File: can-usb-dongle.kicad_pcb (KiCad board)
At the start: 2 copper layers, 30 x 15 mm, 43 parts, among them SW1 SW_PUSH, U1 STM32F302C8T, U2 SN65HVD256, U3 NUF2042XV6, U4 MCP1700, U5 SiP32431, X1 16MHz 10ppm

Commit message: Modify silkscreen text
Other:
- board text added: "CVRA CAN to USB dongle Rev A"
- board text removed: "CAN to USB dongle - Rev A"
- board text removed: "CVRA"
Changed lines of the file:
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@@
     (links 115)
     (no_connects 6)
-    (area 25.087299 28.495199 91.421702 60.2)
+    (area 44.899999 37.399999 75.100001 52.600001)
     (thickness 1.6)
-    (drawings 22)
+    (drawings 21)
     (tracks 470)
     (zones 0)
@@
       (net 10 "Net-(CONN3-Pad6)") (solder_mask_margin 0.2) (clearance 0.3))
   )
-  (gr_text CVRA (at 52.1 51.2 180) (layer B.SilkS)
-    (effects (font (size 0.8 0.8) (thickness 0.2)) (justify mirror))
-  )
   (gr_line (start 46.3 51.15) (end 45.7 51.15) (layer B.SilkS) (width 0.15))
   (gr_line (start 46 50.85) (end 46.3 51.15) (layer B.SilkS) (width 0.15))
@@
     (effects (font (size 0.8 0.8) (thickness 0.2)) (justify mirror))
   )
-  (gr_text "CAN to USB dongle - Rev A" (at 45.75 38.75 180) (layer B.SilkS)
+  (gr_text "CVRA CAN to USB dongle Rev A" (at 45.75 38.75 180) (layer B.SilkS)
     (effects (font (size 0.8 0.8) (thickness 0.15)) (justify left mirror))
   )
-  (gr_text + (at 54.25 50.25) (layer B.SilkS)
-    (effects (font (size 1.5 1.5) (thickness 0.3)) (justify mirror))
+  (gr_text + (at 55.75 51.75) (layer B.SilkS)
+    (effects (font (size 1 1) (thickness 0.2)) (justify mirror))
   )
   (gr_text "+ - TX RX" (at 71.25 38.5 180) (layer B.SilkS)

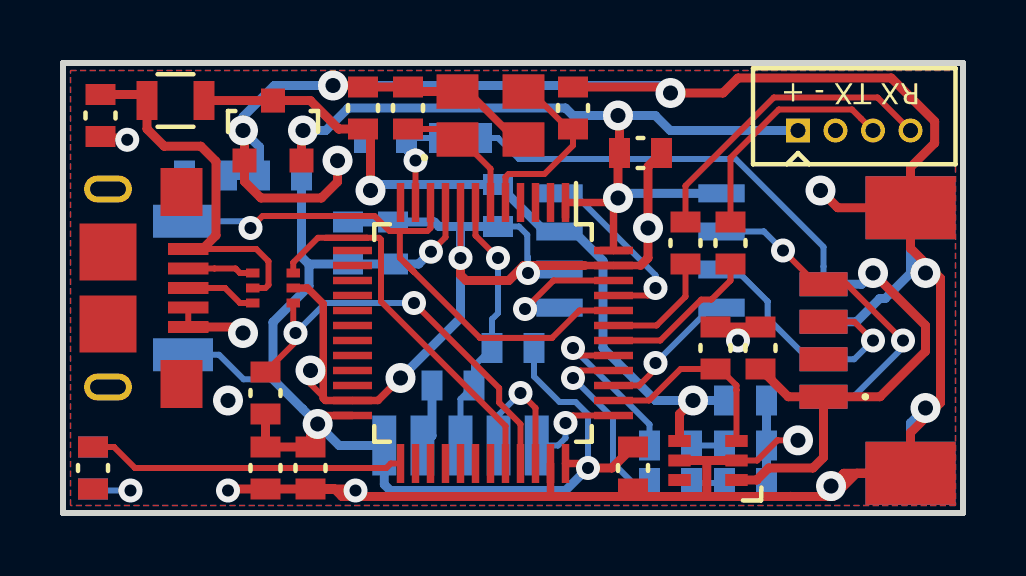
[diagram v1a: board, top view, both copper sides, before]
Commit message: Update footprints (USB, voltage regulator)
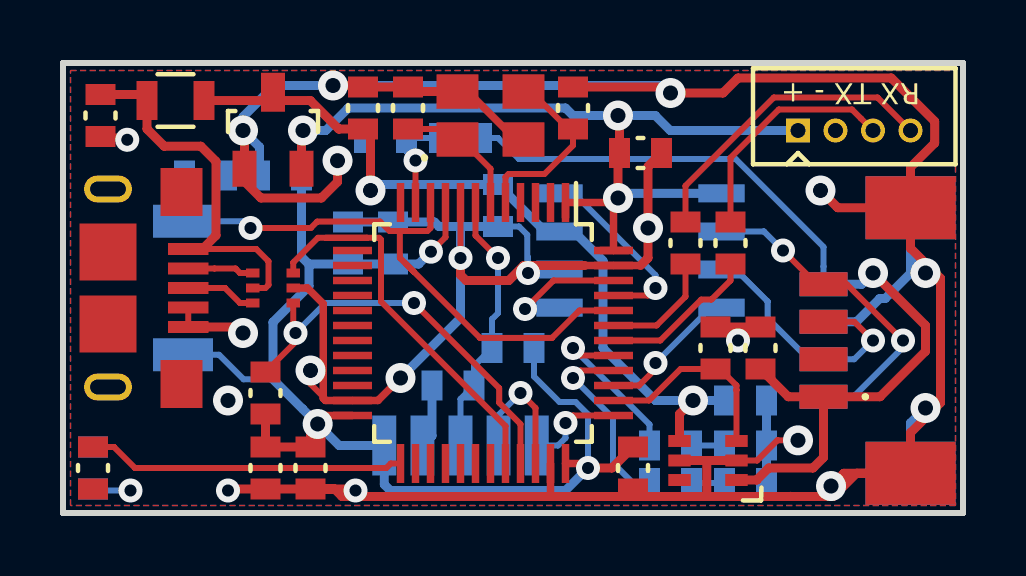
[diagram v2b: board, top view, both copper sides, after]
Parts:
- U4: footprint Housings_SOT-23_SOT-143_TSOT-6:SOT-23 -> _std:SOT-23
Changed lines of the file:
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@@
     (links 115)
     (no_connects 6)
-    (area 44.899999 37.399999 75.100001 52.600001)
+    (area 25.087299 28.495199 91.421702 60.2)
     (thickness 1.6)
     (drawings 21)
-    (tracks 470)
+    (tracks 471)
     (zones 0)
     (modules 43)
@@
       (net 7 "Net-(C13-Pad1)"))
     (model Resistors_SMD.3dshapes/R_0805.wrl
-      (at (xyz 0 0 0))
-      (scale (xyz 1 1 1))
-      (rotate (xyz 0 0 0))
-    )
-  )
-  (module Housings_SOT-23_SOT-143_TSOT-6:SOT-23 (layer F.Cu)
-    (at 52 39.75)
-    (descr "SOT-23, Standard")
-    (tags SOT-23)
-    (attr smd)
-    (fp_text reference U4 (at 0 -2.25) (layer F.SilkS) hide
-      (effects (font (size 1 1) (thickness 0.15)))
-    )
-    (fp_text value MCP1700 (at 0 2.3) (layer F.Fab) hide
-      (effects (font (size 1 1) (thickness 0.15)))
-    )
-    (fp_line (start -1.65 -1.6) (end 1.65 -1.6) (layer F.CrtYd) (width 0.05))
-    (fp_line (start 1.65 -1.6) (end 1.65 1.6) (layer F.CrtYd) (width 0.05))
-    (fp_line (start 1.65 1.6) (end -1.65 1.6) (layer F.CrtYd) (width 0.05))
-    (fp_line (start -1.65 1.6) (end -1.65 -1.6) (layer F.CrtYd) (width 0.05))
-    (fp_line (start 1.29916 -0.65024) (end 1.2509 -0.65024) (layer F.SilkS) (width 0.15))
-    (fp_line (start -1.49982 0.0508) (end -1.49982 -0.65024) (layer F.SilkS) (width 0.15))
-    (fp_line (start -1.49982 -0.65024) (end -1.2509 -0.65024) (layer F.SilkS) (width 0.15))
-    (fp_line (start 1.29916 -0.65024) (end 1.49982 -0.65024) (layer F.SilkS) (width 0.15))
-    (fp_line (start 1.49982 -0.65024) (end 1.49982 0.0508) (layer F.SilkS) (width 0.15))
-    (pad 1 smd rect (at -0.95 1.00076) (size 0.8001 0.8001) (layers F.Cu F.Paste F.Mask)
-      (net 2 GND))
-    (pad 2 smd rect (at 0.95 1.00076) (size 0.8001 0.8001) (layers F.Cu F.Paste F.Mask)
-      (net 1 VCC))
-    (pad 3 smd rect (at 0 -0.99822) (size 0.8001 0.8001) (layers F.Cu F.Paste F.Mask)
-      (net 6 /V_USB))
-    (model Housings_SOT-23_SOT-143_TSOT-6.3dshapes/SOT-23.wrl
       (at (xyz 0 0 0))
       (scale (xyz 1 1 1))
@@
     (pad 6 thru_hole oval (at -3.3 0 270) (size 0.9 1.6) (drill oval 0.5 1.2) (layers *.Cu *.Mask)
       (net 10 "Net-(CONN3-Pad6)") (solder_mask_margin 0.2) (clearance 0.3))
+  )
+  (module _std:SOT-23 (layer F.Cu)
+    (at 52 39.75)
+    (descr "SOT-23, Standard")
+    (tags SOT-23)
+    (attr smd)
+    (fp_text reference U4 (at 0 -3) (layer F.SilkS) hide
+      (effects (font (size 1 1) (thickness 0.15)))
+    )
+    (fp_text value MCP1700 (at 0 3) (layer F.Fab)
+      (effects (font (size 1 1) (thickness 0.15)))
+    )
+    (fp_line (start 1.29916 -0.65024) (end 1.2509 -0.65024) (layer F.SilkS) (width 0.15))
+    (fp_line (start -1.49982 0.0508) (end -1.49982 -0.65024) (layer F.SilkS) (width 0.15))
+    (fp_line (start -1.49982 -0.65024) (end -1.2509 -0.65024) (layer F.SilkS) (width 0.15))
+    (fp_line (start 1.29916 -0.65024) (end 1.49982 -0.65024) (layer F.SilkS) (width 0.15))
+    (fp_line (start 1.49982 -0.65024) (end 1.49982 0.0508) (layer F.SilkS) (width 0.15))
+    (pad 1 smd rect (at -0.95 1.275) (size 0.8 1.2) (layers F.Cu F.Paste F.Mask)
+      (net 2 GND))
+    (pad 2 smd rect (at 0.95 1.275) (size 0.8 1.2) (layers F.Cu F.Paste F.Mask)
+      (net 1 VCC))
+    (pad 3 smd rect (at 0 -1.275) (size 0.8 1.3) (layers F.Cu F.Paste F.Mask)
+      (net 6 /V_USB))
+    (model Housings_SOT-23_SOT-143_TSOT-6.3dshapes/SOT-23.wrl
+      (at (xyz 0 0 0))
+      (scale (xyz 1 1 1))
+      (rotate (xyz 0 0 0))
+    )
   )
   (gr_line (start 46.3 51.15) (end 45.7 51.15) (layer B.SilkS) (width 0.15))
@@
   (segment (start 47.4 51) (end 55.775 51) (width 0.2) (layer F.Cu) (net 13))
   (segment (start 55.925 50.85) (end 56.25 50.85) (width 0.2) (layer F.Cu) (net 13))
+  (segment (start 55.884999 43.100001) (end 55.570568 42.78557) (width 0.2) (layer F.Cu) (net 14))
+  (segment (start 51.25 43) (end 53.259301 43) (width 0.2) (layer F.Cu) (net 14))
+  (segment (start 53.259301 43) (end 53.473731 42.78557) (width 0.2) (layer F.Cu) (net 14))
+  (segment (start 53.473731 42.78557) (end 55.570568 42.78557) (width 0.2) (layer F.Cu) (net 14))
   (segment (start 56.229049 43.100001) (end 55.884999 43.100001) (width 0.2) (layer F.Cu) (net 14))
   (segment (start 57.149999 43.100001) (end 56.229049 43.100001) (width 0.2) (layer F.Cu) (net 14))
@@
   (segment (start 49 42.775) (end 51.025 42.775) (width 0.2) (layer B.Cu) (net 14))
   (segment (start 51.025 42.775) (end 51.25 43) (width 0.2) (layer B.Cu) (net 14))
-  (segment (start 55.884999 43.100001) (end 55.384999 42.600001) (width 0.2) (layer F.Cu) (net 14))
-  (segment (start 55.384999 42.600001) (end 51.649999 42.600001) (width 0.2) (layer F.Cu) (net 14))
-  (segment (start 51.649999 42.600001) (end 51.25 43) (width 0.2) (layer F.Cu) (net 14))
   (segment (start 57.149999 43.100001) (end 57.25 43) (width 0.2) (layer F.Cu) (net 14))
   (segment (start 57.25 43) (end 57.25 42.15) (width 0.2) (layer F.Cu) (net 14))

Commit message: Resolve GPIO conflict with JTAG pin
V_BUS_ENABLE and CAN_SILENT were in conflict with JTAG output pins.
They had to be moved because at boot time the output value cannot be guaranteed.
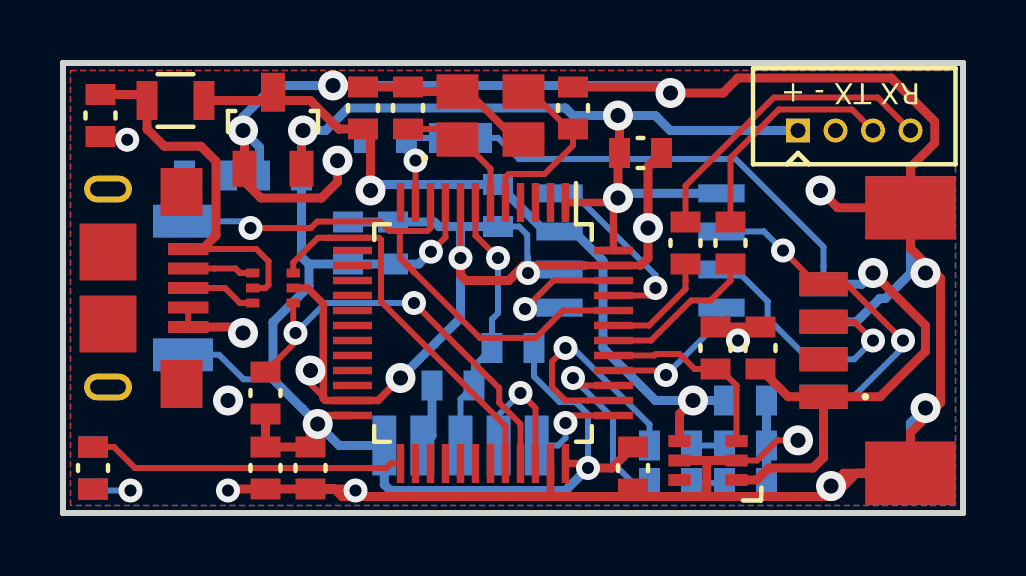
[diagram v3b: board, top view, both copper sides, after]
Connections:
- U1 pad 38: /V_BUS_ENABLE -> /CAN1_PWR_LED
- U1 pad 39: /CAN_SILENT -> /CAN1_STATUS_LED
- U1 pad 40: /CAN1_STATUS_LED -> /CAN_SILENT
- U1 pad 41: /CAN1_PWR_LED -> /V_BUS_ENABLE
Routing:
- net /CAN1_PWR_LED: track 5.76 -> 8.28 mm
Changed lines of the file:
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@@
     (links 115)
     (no_connects 6)
-    (area 25.087299 28.495199 91.421702 60.2)
+    (area 44.899999 37.399999 75.100001 52.600001)
     (thickness 1.6)
     (drawings 21)
-    (tracks 471)
+    (tracks 475)
     (zones 0)
     (modules 43)
@@
       (net 8 /SWCLK))
     (pad 38 smd rect (at 2.25 -4.35) (size 1.3 0.25) (layers F.Cu F.Paste F.Mask)
+      (net 27 /CAN1_PWR_LED))
+    (pad 39 smd rect (at 1.75 -4.35) (size 1.3 0.25) (layers F.Cu F.Paste F.Mask)
+      (net 26 /CAN1_STATUS_LED))
+    (pad 40 smd rect (at 1.25 -4.35) (size 1.3 0.25) (layers F.Cu F.Paste F.Mask)
+      (net 24 /CAN_SILENT))
+    (pad 41 smd rect (at 0.75 -4.35) (size 1.3 0.25) (layers F.Cu F.Paste F.Mask)
       (net 17 /V_BUS_ENABLE))
-    (pad 39 smd rect (at 1.75 -4.35) (size 1.3 0.25) (layers F.Cu F.Paste F.Mask)
-      (net 24 /CAN_SILENT))
-    (pad 40 smd rect (at 1.25 -4.35) (size 1.3 0.25) (layers F.Cu F.Paste F.Mask)
-      (net 26 /CAN1_STATUS_LED))
-    (pad 41 smd rect (at 0.75 -4.35) (size 1.3 0.25) (layers F.Cu F.Paste F.Mask)
-      (net 27 /CAN1_PWR_LED))
     (pad 42 smd rect (at 0.25 -4.35) (size 1.3 0.25) (layers F.Cu F.Paste F.Mask)
       (net 21 /UART1_TX))
@@
   (segment (start 47.4 51) (end 55.775 51) (width 0.2) (layer F.Cu) (net 13))
   (segment (start 55.925 50.85) (end 56.25 50.85) (width 0.2) (layer F.Cu) (net 13))
+  (segment (start 60.760083 46.663999) (end 58.900001 46.663999) (width 0.2) (layer F.Cu) (net 14))
+  (segment (start 63.35 45.75) (end 61.674082 45.75) (width 0.2) (layer F.Cu) (net 14))
+  (segment (start 61.674082 45.75) (end 60.760083 46.663999) (width 0.2) (layer F.Cu) (net 14))
+  (segment (start 58.900001 46.663999) (end 56.689849 44.453847) (width 0.2) (layer F.Cu) (net 14))
   (segment (start 55.884999 43.100001) (end 55.570568 42.78557) (width 0.2) (layer F.Cu) (net 14))
   (segment (start 51.25 43) (end 53.259301 43) (width 0.2) (layer F.Cu) (net 14))
@@
   (segment (start 56.229049 43.100001) (end 55.884999 43.100001) (width 0.2) (layer F.Cu) (net 14))
   (segment (start 57.149999 43.100001) (end 56.229049 43.100001) (width 0.2) (layer F.Cu) (net 14))
-  (segment (start 58.900001 46.663999) (end 56.689849 44.453847) (width 0.2) (layer F.Cu) (net 14))
   (segment (start 56.689849 44.453847) (end 56.4234 44.187398) (width 0.2) (layer F.Cu) (net 14))
   (segment (start 56.229049 43.100001) (end 56.229049 43.993047) (width 0.2) (layer F.Cu) (net 14))
   (segment (start 56.229049 43.993047) (end 56.689849 44.453847) (width 0.2) (layer F.Cu) (net 14))
-  (segment (start 63.35 45.75) (end 62.213998 45.75) (width 0.2) (layer F.Cu) (net 14))
-  (segment (start 62.213998 45.75) (end 61.299999 46.663999) (width 0.2) (layer F.Cu) (net 14))
-  (segment (start 61.299999 46.663999) (end 58.900001 46.663999) (width 0.2) (layer F.Cu) (net 14))
   (segment (start 49.05 41.25) (end 49.05 42.725) (width 0.2) (layer B.Cu) (net 14))
   (segment (start 49.05 42.725) (end 49 42.775) (width 0.2) (layer B.Cu) (net 14))
@@
   (segment (start 52.675 46.425) (end 52.75 46.5) (width 0.2) (layer F.Cu) (net 16))
   (via (at 52.75 46.5) (size 0.8) (drill 0.4) (layers F.Cu B.Cu) (net 16))
-  (segment (start 63.35 48.75) (end 64.536002 48.75) (width 0.2) (layer F.Cu) (net 17))
-  (segment (start 64.536002 48.75) (end 65.586002 47.7) (width 0.2) (layer F.Cu) (net 17))
-  (segment (start 65.586002 47.7) (end 66.05 47.7) (width 0.2) (layer F.Cu) (net 17))
+  (segment (start 63.35 47.25) (end 64.713998 47.25) (width 0.2) (layer F.Cu) (net 17))
+  (segment (start 64.713998 47.25) (end 64.763999 47.199999) (width 0.2) (layer F.Cu) (net 17))
+  (segment (start 64.763999 47.199999) (end 65.549999 47.199999) (width 0.2) (layer F.Cu) (net 17))
+  (segment (start 65.549999 47.199999) (end 66.05 47.7) (width 0.2) (layer F.Cu) (net 17))
   (segment (start 66.05 47.7) (end 66.75 47.7) (width 0.2) (layer F.Cu) (net 17))
   (segment (start 67.44996 50.09976) (end 67.44996 48.39996) (width 0.2) (layer F.Cu) (net 17))
@@
   (segment (start 60.445 45.655) (end 60.4 45.7) (width 0.2) (layer B.Cu) (net 19))
   (via (at 60.4 45.7) (size 0.8) (drill 0.4) (layers F.Cu B.Cu) (net 19))
-  (segment (start 65.75 45.286002) (end 65.75 44.2) (width 0.2) (layer F.Cu) (net 20))
-  (segment (start 64.786002 46.25) (end 65.75 45.286002) (width 0.2) (layer F.Cu) (net 20))
-  (segment (start 63.35 46.25) (end 64.786002 46.25) (width 0.2) (layer F.Cu) (net 20))
+  (segment (start 63.35 46.25) (end 64.536002 46.25) (width 0.2) (layer F.Cu) (net 20))
+  (segment (start 64.536002 46.25) (end 65.75 45.036002) (width 0.2) (layer F.Cu) (net 20))
+  (segment (start 65.75 45.036002) (end 65.75 44.75) (width 0.2) (layer F.Cu) (net 20))
+  (segment (start 65.75 44.75) (end 65.75 44.2) (width 0.2) (layer F.Cu) (net 20))
   (segment (start 67.25 44.2) (end 67.25 44.75) (width 0.2) (layer F.Cu) (net 21))
-  (segment (start 67.25 44.75) (end 66.614277 45.385723) (width 0.2) (layer F.Cu) (net 21))
-  (segment (start 66.614277 45.385723) (end 66.274275 45.385723) (width 0.2) (layer F.Cu) (net 21))
-  (segment (start 64.909998 46.75) (end 66.274275 45.385723) (width 0.2) (layer F.Cu) (net 21))
-  (segment (start 63.35 46.75) (end 64.909998 46.75) (width 0.2) (layer F.Cu) (net 21))
+  (segment (start 67.25 44.75) (end 66.586465 45.413535) (width 0.2) (layer F.Cu) (net 21))
+  (segment (start 66.586465 45.413535) (end 65.938165 45.413535) (width 0.2) (layer F.Cu) (net 21))
+  (segment (start 65.938165 45.413535) (end 64.6017 46.75) (width 0.2) (layer F.Cu) (net 21))
+  (segment (start 64.6017 46.75) (end 63.35 46.75) (width 0.2) (layer F.Cu) (net 21))
   (segment (start 51.325 44.5) (end 50.9 44.5) (width 0.2) (layer F.Cu) (net 22))
   (segment (start 50.75 44.35) (end 50.05 44.35) (width 0.2) (layer F.Cu) (net 22))
@@
   (segment (start 50.4 45) (end 50.05 45) (width 0.2) (layer F.Cu) (net 23))
   (segment (start 50.05 45) (end 49.175 45) (width 0.2) (layer F.Cu) (net 23))
-  (segment (start 64.75 47.5) (end 66.595 45.655) (width 0.2) (layer B.Cu) (net 24))
-  (segment (start 66.595 45.655) (end 66.95 45.655) (width 0.2) (layer B.Cu) (net 24))
-  (segment (start 63.35 48.25) (end 64.2 48.25) (width 0.2) (layer F.Cu) (net 24))
-  (segment (start 64.2 48.25) (end 64.75 47.7) (width 0.2) (layer F.Cu) (net 24))
-  (segment (start 64.75 47.7) (end 64.75 47.5) (width 0.2) (layer F.Cu) (net 24))
-  (via (at 64.75 47.5) (size 0.8) (drill 0.4) (layers F.Cu B.Cu) (net 24))
-  (segment (start 66.845 45.655) (end 66.95 45.655) (width 0.2) (layer B.Cu) (net 24))
+  (segment (start 65.1 47.9) (end 66.95 46.05) (width 0.2) (layer B.Cu) (net 24))
+  (segment (start 66.95 46.05) (end 66.95 45.655) (width 0.2) (layer B.Cu) (net 24))
+  (segment (start 65.1 47.9) (end 64.95 47.75) (width 0.2) (layer F.Cu) (net 24))
+  (segment (start 64.95 47.75) (end 63.35 47.75) (width 0.2) (layer F.Cu) (net 24))
+  (via (at 65.1 47.9) (size 0.8) (drill 0.4) (layers F.Cu B.Cu) (net 24))
   (segment (start 59.75 50.85) (end 59.75 49.601699) (width 0.2) (layer F.Cu) (net 25))
   (segment (start 59.75 49.601699) (end 55.600001 45.4517) (width 0.2) (layer F.Cu) (net 25))
@@
   (segment (start 52.675 44.15) (end 53.500001 43.324999) (width 0.2) (layer F.Cu) (net 25))
   (segment (start 53.500001 43.324999) (end 55.137313 43.324999) (width 0.2) (layer F.Cu) (net 25))
+  (segment (start 62 48) (end 62.25 48.25) (width 0.2) (layer F.Cu) (net 26))
+  (segment (start 62.25 48.25) (end 63.35 48.25) (width 0.2) (layer F.Cu) (net 26))
   (segment (start 62 48) (end 63.332834 49.332834) (width 0.2) (layer B.Cu) (net 26))
   (segment (start 64.55 51.5) (end 64 51.5) (width 0.2) (layer B.Cu) (net 26))
   (segment (start 64 51.5) (end 63.332834 50.832834) (width 0.2) (layer B.Cu) (net 26))
   (segment (start 63.332834 50.832834) (end 63.332834 49.332834) (width 0.2) (layer B.Cu) (net 26))
-  (segment (start 63.35 47.75) (end 62.25 47.75) (width 0.2) (layer F.Cu) (net 26))
-  (segment (start 62.25 47.75) (end 62 48) (width 0.2) (layer F.Cu) (net 26))
   (via (at 62 48) (size 0.8) (drill 0.4) (layers F.Cu B.Cu) (net 26))
+  (segment (start 61.75 47) (end 61.299999 47.450001) (width 0.2) (layer F.Cu) (net 27))
+  (segment (start 61.299999 47.450001) (end 61.299999 48.299999) (width 0.2) (layer F.Cu) (net 27))
+  (segment (start 61.299999 48.299999) (end 61.75 48.75) (width 0.2) (layer F.Cu) (net 27))
+  (segment (start 61.75 48.75) (end 62.5 48.75) (width 0.2) (layer F.Cu) (net 27))
+  (segment (start 62.5 48.75) (end 63.35 48.75) (width 0.2) (layer F.Cu) (net 27))
+  (segment (start 62 47) (end 61.75 47) (width 0.2) (layer B.Cu) (net 27))
+  (via (at 61.75 47) (size 0.8) (drill 0.4) (layers F.Cu B.Cu) (net 27))
   (segment (start 62 47) (end 64.55 49.55) (width 0.2) (layer B.Cu) (net 27))
   (segment (start 64.55 49.55) (end 64.55 50.25) (width 0.2) (layer B.Cu) (net 27))
-  (segment (start 63.35 47.25) (end 62.25 47.25) (width 0.2) (layer F.Cu) (net 27))
-  (segment (start 62.25 47.25) (end 62 47) (width 0.2) (layer F.Cu) (net 27))
-  (via (at 62 47) (size 0.8) (drill 0.4) (layers F.Cu B.Cu) (net 27))
   (segment (start 67.25 42.8) (end 67.25 40.659998) (width 0.2) (layer F.Cu) (net 28))
   (segment (start 71.600001 39.350001) (end 72 39.75) (width 0.2) (layer F.Cu) (net 28))

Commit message: Fix floating via
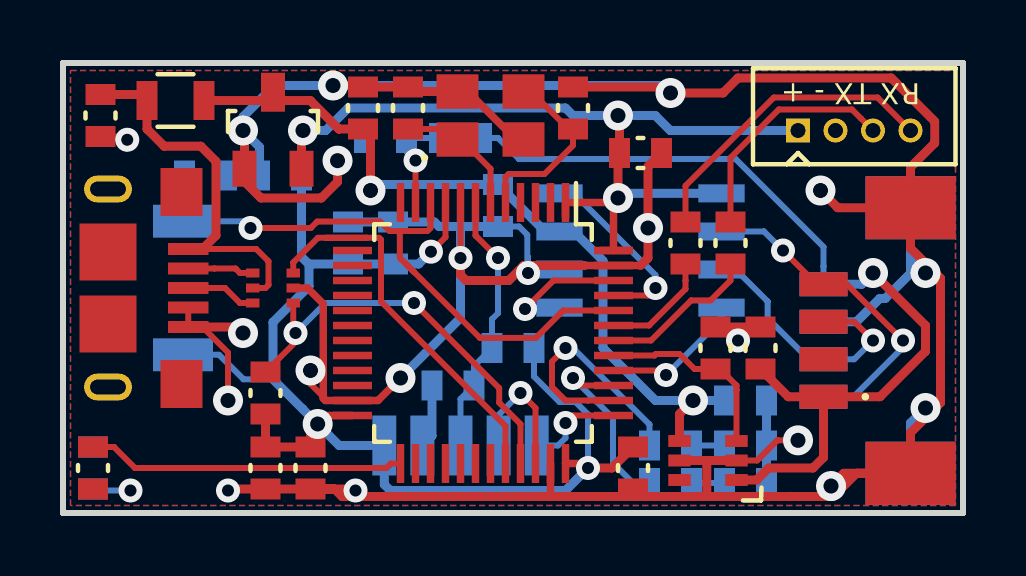
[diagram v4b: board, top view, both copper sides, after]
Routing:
- net GND: track 155.2 -> 158.5 mm, vias 19 -> 20
- net (no net): vias 1 -> 0
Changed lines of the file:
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@@
     (thickness 1.6)
     (drawings 21)
-    (tracks 475)
+    (tracks 478)
     (zones 0)
     (modules 43)
@@
   (gr_line (start 45 52.5) (end 75 52.5) (layer Edge.Cuts) (width 0.2))
   (gr_line (start 45 37.5) (end 45 52.5) (layer Edge.Cuts) (width 0.2))
-  (via (at 50.5 48.75) (size 1) (drill 0.5) (layers F.Cu B.Cu) (net 0))
   (segment (start 28.3079 28.8202) (end 28.1174 29.0107) (width 0.25) (layer Dwgs.User) (net 0))
   (segment (start 25.4123 31.7158) (end 28.3079 28.8202) (width 0.25) (layer Dwgs.User) (net 0))
@@
   (segment (start 61.769981 50.869981) (end 61.75 50.85) (width 0.25) (layer F.Cu) (net 1))
   (via (at 62.5 51) (size 0.8) (drill 0.4) (layers F.Cu B.Cu) (net 1))
+  (segment (start 49.175 46.3) (end 49.65 46.3) (width 0.2) (layer F.Cu) (net 2))
+  (segment (start 49.65 46.3) (end 50.5 47.15) (width 0.2) (layer F.Cu) (net 2))
+  (segment (start 50.5 47.15) (end 50.5 48.75) (width 0.2) (layer F.Cu) (net 2))
+  (via (at 50.5 48.75) (size 1) (drill 0.5) (layers F.Cu B.Cu) (net 2))
   (segment (start 56.25 48) (end 58.25 46) (width 0.3) (layer B.Cu) (net 2))
   (segment (start 58.25 46) (end 58.25 44) (width 0.3) (layer B.Cu) (net 2))
